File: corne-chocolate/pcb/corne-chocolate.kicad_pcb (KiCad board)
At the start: 2 copper layers, 116.2 x 91.4 mm, 82 parts, among them J1 MJ-4PP-9, J2 Conn_01x04, J3 Conn_01x03, P1 Conn_01x01, P2 Conn_01x01, SW10 SW_PUSH, SW11 SW_PUSH, SW12 SW_PUSH, SW14 SW_PUSH, SW15 SW_PUSH, SW16 SW_PUSH, SW17 SW_PUSH, SW18 SW_PUSH, SW19 SW_PUSH, SW2 SW_PUSH, SW20 SW_PUSH, SW21 SW_PUSH, SW3 SW_PUSH, SW4 SW_PUSH, SW5 SW_PUSH, SW6 SW_PUSH, SW8 SW_PUSH, SW9 SW_PUSH, U1 ProMicro

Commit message: finishes routing
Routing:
- added copper zone on B.Cu, net (none)
- removed copper zone on B.Cu, net Net-(D18-A)
- removed copper zone on B.Cu, net Net-(L12-DIN)
- removed copper zone on B.Cu, net Net-(L14-DOUT)

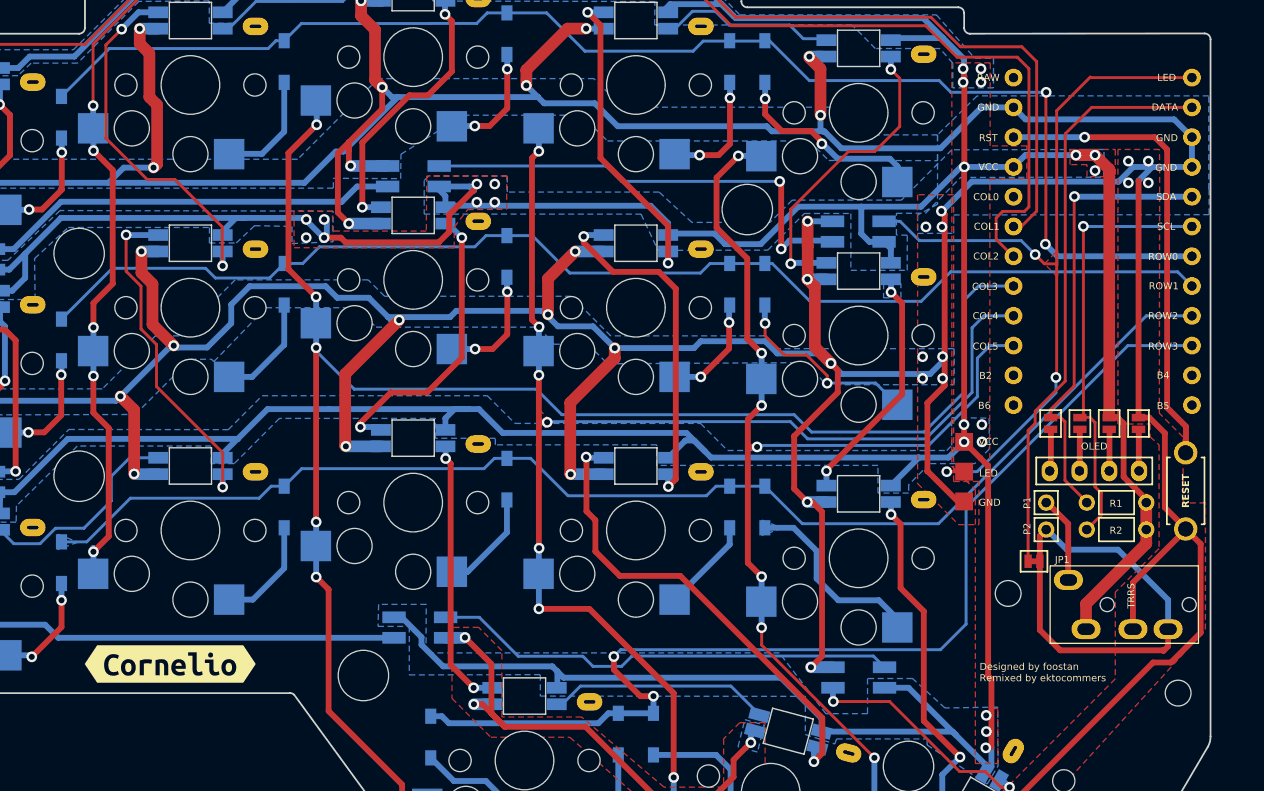
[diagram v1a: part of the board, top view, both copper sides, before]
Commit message: updates some footprints
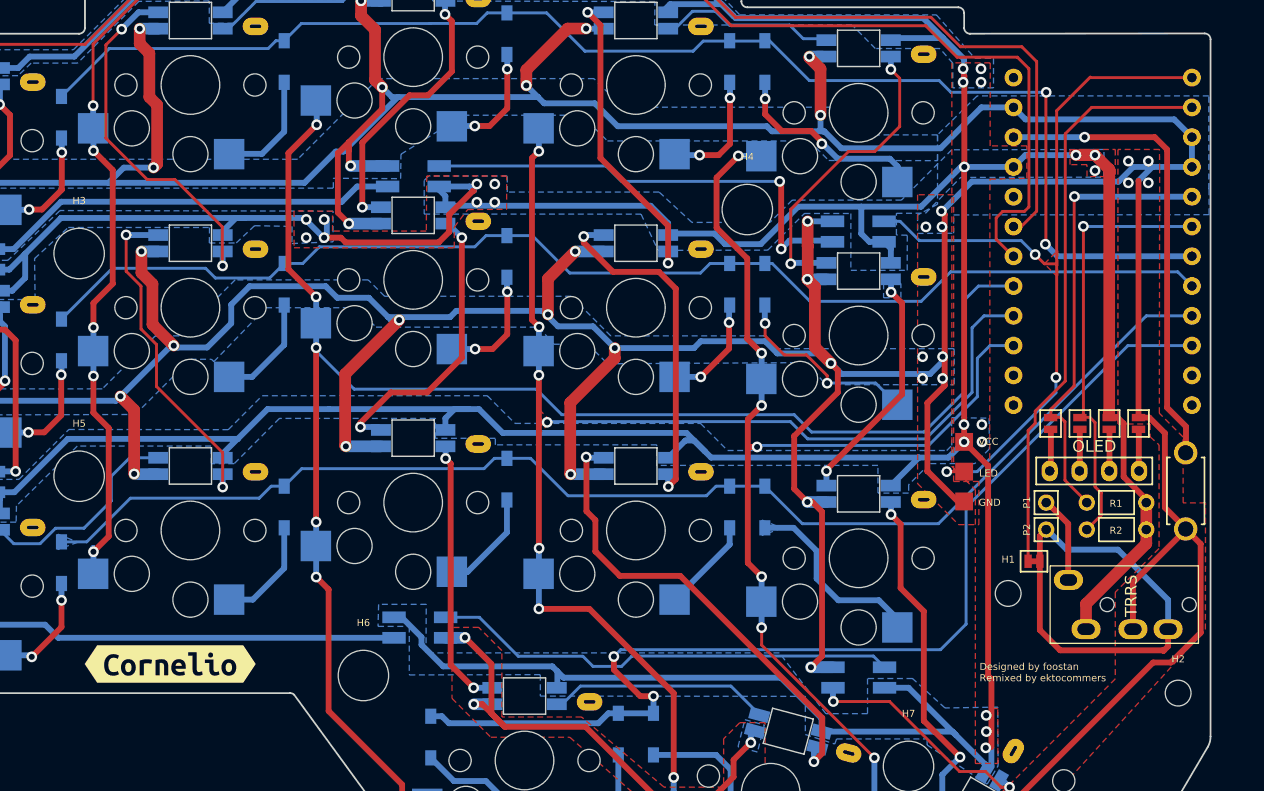
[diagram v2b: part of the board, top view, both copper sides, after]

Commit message: reannotates
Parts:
- removed J3: Conn_01x03, kbd:StripLED_1side
- removed JP1: Device:Jumper, kbd:Jumper
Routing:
- net LED: track 66.7 -> 39.2 mm, vias 3 -> 1
- net GND: track 639.5 -> 627.4 mm
- net data: track 88.0 -> 85.0 mm
- net row0: track 116.4 -> 116.9 mm
- net SCL: track 37.0 -> 36.5 mm
- removed copper zone on F.Cu, net LED
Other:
- board text removed: "GND"
- board text removed: "LED"
- board text removed: "VCC"

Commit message: starts component review
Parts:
- D10, D11, D12, D14, D15, D16, D17, D18, D19, D2, D20, D21, D3, D4, D5, D6, D8, D9: value D -> 1N4148W; footprint kbd:D3_SMD -> kbd:D_SOD-123
- moved D2 0.09 mm to (97.0, 75.2)

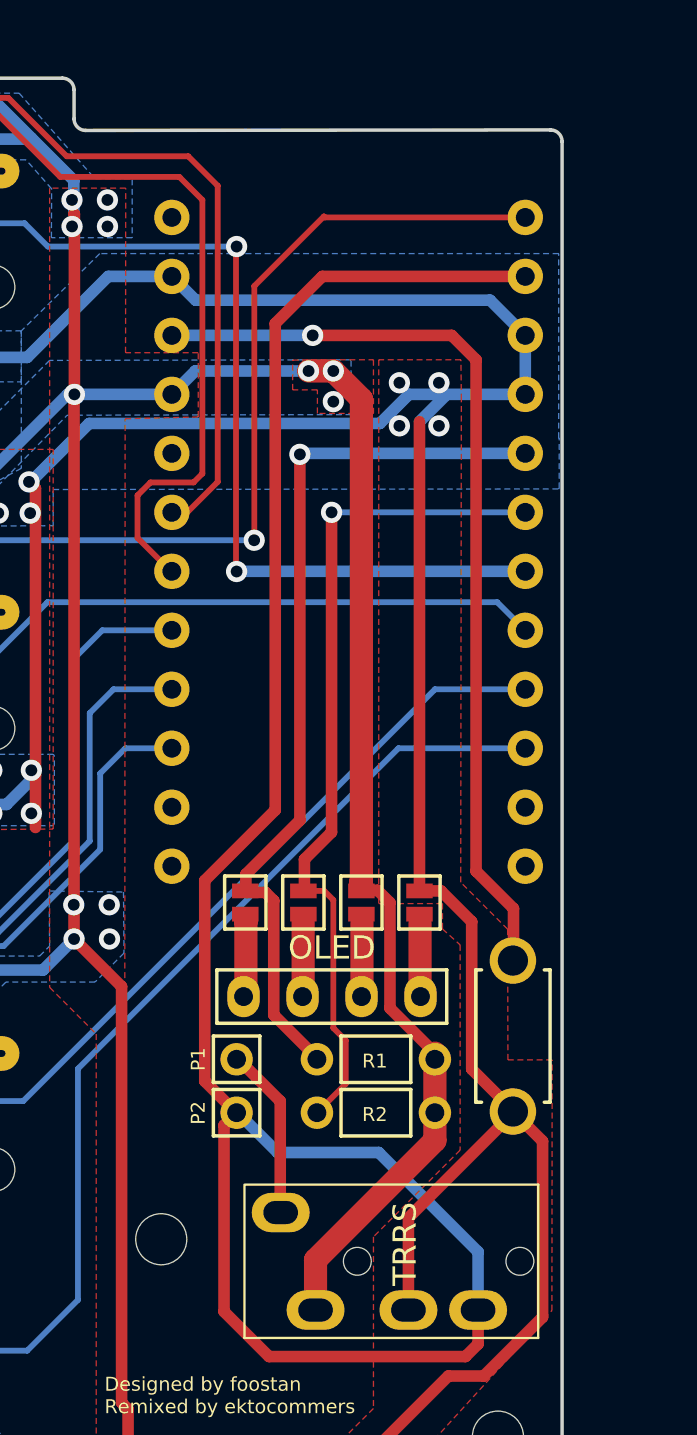
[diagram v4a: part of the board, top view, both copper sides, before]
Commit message: switch to nrf52840 micro. All items from amazon
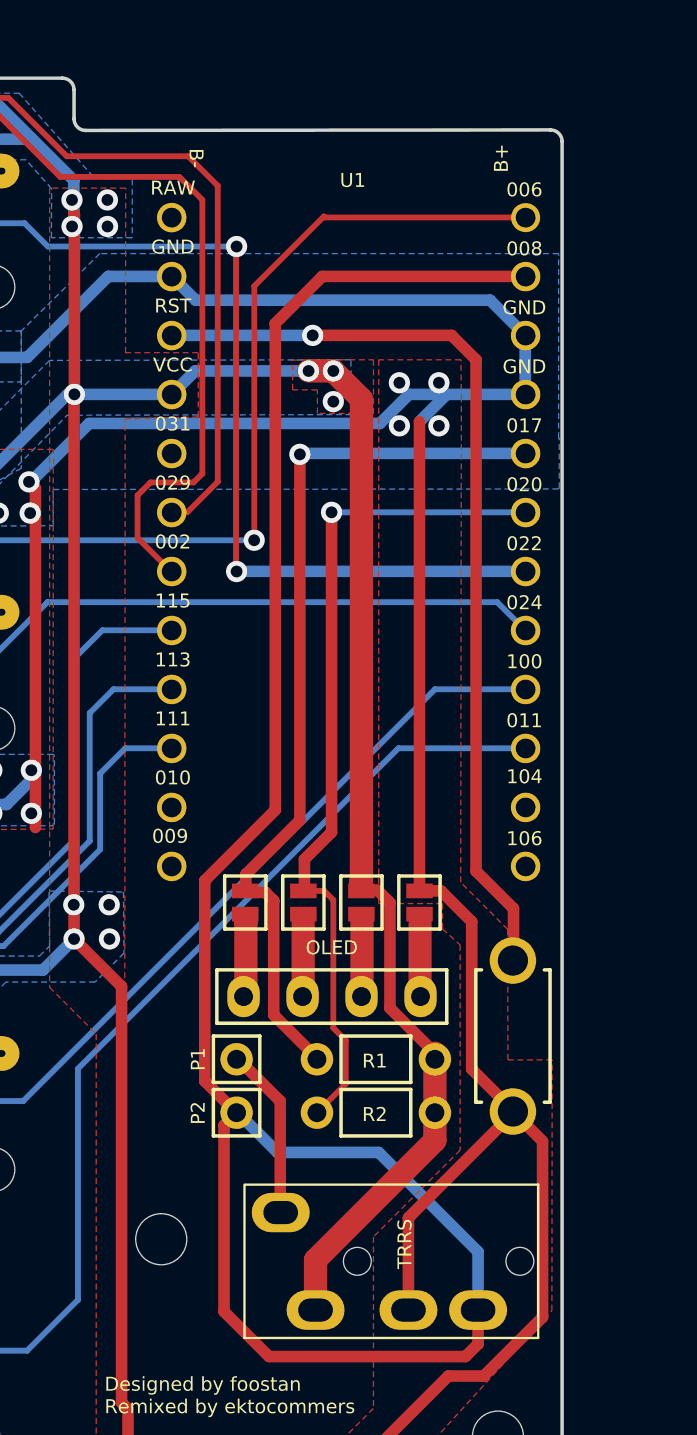
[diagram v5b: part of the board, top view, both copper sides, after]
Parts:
- U1: value ProMicro -> nrf52840; footprint kbd:ProMicro_v2_1side -> kbd:nrf52840
- moved U1 16.5 mm to (186.5, 102.7)

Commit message: adds right keyboard
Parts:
- added D13: 1N4148W, kbd:D_SOD-123, F.Cu at (247.7, 90.2)
- added D22: 1N4148W, kbd:D_SOD-123, F.Cu at (247.7, 109.2)
- added D23: 1N4148W, kbd:D_SOD-123, F.Cu at (228.7, 66.6)
- added D24: 1N4148W, kbd:D_SOD-123, F.Cu at (228.7, 85.5)
- added D25: 1N4148W, kbd:D_SOD-123, F.Cu at (228.7, 104.4)
- added D26: 1N4148W, kbd:D_SOD-123, F.Cu at (209.7, 64.2)
- added D27: 1N4148W, kbd:D_SOD-123, F.Cu at (209.7, 83.2)
- added D28: 1N4148W, kbd:D_SOD-123, F.Cu at (209.7, 102.0)
- added D29: 1N4148W, kbd:D_SOD-123, F.Cu at (216.2, 124.1)
- added D30: 1N4148W, kbd:D_SOD-123, F.Cu at (190.7, 66.5)
- added D31: 1N4148W, kbd:D_SOD-123, F.Cu at (190.7, 85.5)
- added D32: 1N4148W, kbd:D_SOD-123, F.Cu at (190.7, 104.5)
- added D33: 1N4148W, kbd:D_SOD-123, F.Cu at (200.2, 123.9)
- added D34: 1N4148W, kbd:D_SOD-123, F.Cu at (187.7, 66.4)
- added D35: 1N4148W, kbd:D_SOD-123, F.Cu at (187.7, 85.5)
- added D36: 1N4148W, kbd:D_SOD-123, F.Cu at (187.7, 104.4)
- added D37: 1N4148W, kbd:D_SOD-123, F.Cu at (197.2, 123.8)
- added D7: 1N4148W, kbd:D_SOD-123, F.Cu at (247.8, 71.3)
- added H10: MountingHole, MountingHole:MountingHole_2.2mm_M2_ISO14580, F.Cu at (152.5, 120.4)
- added H11: MountingHole, MountingHole:MountingHole_4.3mm_M4_ISO14580, F.Cu at (222.0, 118.9)
- added H12: MountingHole, MountingHole:MountingHole_2.2mm_M2_ISO14580, F.Cu at (167.0, 111.9)
- added H13: MountingHole, MountingHole:MountingHole_4.3mm_M4_ISO14580, F.Cu at (246.2, 101.9)
- added H14: MountingHole, MountingHole:MountingHole_4.3mm_M4_ISO14580, F.Cu at (246.2, 82.9)
- added H7, H8: MountingHole, MountingHole:MountingHole_4.3mm_M4_ISO14580, F.Cu at (175.5, 126.6)
- added H9: MountingHole, MountingHole:MountingHole_4.3mm_M4_ISO14580, F.Cu at (189.2, 79.1)
- added J3: MJ-4PP-9, kbd:MJ-4PP-9_1side, F.Cu at (150.0, 112.8)
- added J4: Conn_01x04, kbd:OLED_1side, F.Cu at (155.8, 101.4)
- added JP6: Device:Jumper_NO_Small, kbd:Jumper, F.Cu at (155.9, 97.4)
- added JP7: Device:Jumper_NO_Small, kbd:Jumper, F.Cu at (158.3, 97.4)
- added JP8: Device:Jumper_NO_Small, kbd:Jumper, F.Cu at (160.9, 97.4)
- added JP9: Device:Jumper_NO_Small, kbd:Jumper, F.Cu at (163.3, 97.4)
- added L10, L37: SK6812MINI, kbd:YS-SK6812MINI-E, F.Cu at (217.7, 79.6)
- added L13: SK6812MINI, kbd:YS-SK6812MINI-E, F.Cu at (255.7, 86.7)
- added L28: SK6812MINI, kbd:SK6812MINI_underglow_rev, F.Cu at (255.7, 83.4)
- added L29: SK6812MINI, kbd:SK6812MINI_underglow_rev, F.Cu at (255.7, 102.3)
- added L30: SK6812MINI, kbd:YS-SK6812MINI-E, F.Cu at (255.8, 105.8)
- added L31: SK6812MINI, kbd:YS-SK6812MINI-E, F.Cu at (236.7, 62.9)
- added L32: SK6812MINI, kbd:YS-SK6812MINI-E, F.Cu at (236.7, 82.0)
- added L33: SK6812MINI, kbd:YS-SK6812MINI-E, F.Cu at (236.8, 101.0)
- added L34: SK6812MINI, kbd:SK6812MINI_underglow_rev, F.Cu at (217.7, 76.3)
- added L35: SK6812MINI, kbd:SK6812MINI_underglow_rev, F.Cu at (217.2, 114.8)
- added L36: SK6812MINI, kbd:YS-SK6812MINI-E, F.Cu at (217.8, 60.6)
- added L38: SK6812MINI, kbd:YS-SK6812MINI-E, F.Cu at (217.8, 98.6)
- added L39: SK6812MINI, kbd:YS-SK6812MINI-E, F.Cu at (208.3, 120.6)
- added L4: SK6812MINI, kbd:YS-SK6812MINI-E, F.Cu at (217.7, 60.6)
- added L40: SK6812MINI, kbd:YS-SK6812MINI-E, F.Cu at (198.7, 62.9)
- added L41: SK6812MINI, kbd:YS-SK6812MINI-E, F.Cu at (198.8, 82.0)
- added L42: SK6812MINI, kbd:YS-SK6812MINI-E, F.Cu at (198.7, 100.9)
- added L43: SK6812MINI, kbd:YS-SK6812MINI-E, F.Cu at (185.7, 123.6)
- added L44: SK6812MINI, kbd:SK6812MINI_underglow_rev, F.Cu at (179.8, 81.0)
- added L45: SK6812MINI, kbd:SK6812MINI_underglow_rev, F.Cu at (179.7, 119.0)
- added L46: SK6812MINI, kbd:YS-SK6812MINI-E, F.Cu at (179.7, 65.4)
- added L47: SK6812MINI, kbd:YS-SK6812MINI-E, F.Cu at (179.7, 84.4)
- added L48: SK6812MINI, kbd:YS-SK6812MINI-E, F.Cu at (179.7, 103.4)
- added L49: SK6812MINI, kbd:YS-SK6812MINI-E, F.Cu at (169.7, 129.9)
- added L5: SK6812MINI, kbd:YS-SK6812MINI-E, F.Cu at (198.7, 63.0)
- added L7: SK6812MINI, kbd:YS-SK6812MINI-E, F.Cu at (255.7, 67.7)
- added P3: Conn_01x01, kbd:1pin_conn, F.Cu at (163.7, 104.1)
- added P4: Conn_01x01, kbd:1pin_conn, F.Cu at (163.7, 106.4)
- added R3: R, kbd:R, F.Cu at (157.7, 104.1)
- added R4: R, kbd:R, F.Cu at (157.7, 106.4)
- added RSW2: SW_PUSH, kbd:ResetSW_1side, F.Cu at (151.8, 103.1)
- added SW13: SW_PUSH, kbd:ChocV1_V2_Hotswap, F.Cu at (255.7, 92.2)
- added SW22: SW_PUSH, kbd:ChocV1_V2_Hotswap, F.Cu at (255.7, 111.2)
- added SW23: SW_PUSH, kbd:ChocV1_V2_Hotswap, F.Cu at (236.7, 68.5)
- added SW24: SW_PUSH, kbd:ChocV1_V2_Hotswap, F.Cu at (236.7, 87.5)
- added SW25: SW_PUSH, kbd:ChocV1_V2_Hotswap, F.Cu at (236.7, 106.5)
- added SW26: SW_PUSH, kbd:ChocV1_V2_Hotswap, F.Cu at (217.7, 66.1)
- added SW27: SW_PUSH, kbd:ChocV1_V2_Hotswap, F.Cu at (217.7, 85.1)
- added SW28: SW_PUSH, kbd:ChocV1_V2_Hotswap, F.Cu at (217.7, 104.1)
- added SW29: SW_PUSH, kbd:ChocV1_V2_Hotswap, F.Cu at (208.2, 126.1)
- added SW30: SW_PUSH, kbd:ChocV1_V2_Hotswap, F.Cu at (198.7, 68.5)
- added SW31: SW_PUSH, kbd:ChocV1_V2_Hotswap, F.Cu at (198.7, 87.5)
- added SW32: SW_PUSH, kbd:ChocV1_V2_Hotswap, F.Cu at (198.7, 106.5)
- added SW33: SW_PUSH, kbd:ChocV1_V2_Hotswap, F.Cu at (187.2, 128.9)
- added SW34: SW_PUSH, kbd:ChocV1_V2_Hotswap, F.Cu at (179.7, 70.9)
- added SW35: SW_PUSH, kbd:ChocV1_V2_Hotswap, F.Cu at (179.7, 89.9)
- added SW36: SW_PUSH, kbd:ChocV1_V2_Hotswap, F.Cu at (179.7, 108.9)
- added SW37: SW_PUSH, kbd:ChocV1_V2_Hotswap_1.5u, F.Cu at (165.0, 132.6)
- added SW7: SW_PUSH, kbd:ChocV1_V2_Hotswap, F.Cu at (255.7, 73.2)
- added U2: ProMicro, kbd:ProMicro_v2_1side, F.Cu at (158.9, 82.3)
- added kibuzzard-65BBD98A: G***, kibuzzard-65BBD98A, F.Cu at (238.5, 117.9)
- U1: value nrf52840 -> ProMicro; footprint kbd:nrf52840 -> kbd:ProMicro_v2_1side
- moved U1 54.1 mm to (136.4, 82.3)
- moved kibuzzard-65BBD98A 49.5 mm to (56.9, 117.9)
- moved D10 49.5 mm to (85.6, 83.1)
- moved D11 49.5 mm to (104.6, 85.5)
- moved D12 49.5 mm to (107.6, 85.5)
- moved D14 49.5 mm to (47.6, 109.2)
- moved D15 49.5 mm to (66.6, 104.5)
- moved D16 49.5 mm to (85.6, 102.1)
- moved D17 49.5 mm to (104.6, 104.5)
- moved D18 49.5 mm to (107.6, 104.5)
- moved D19 49.5 mm to (79.1, 124.1)
- moved D2 49.5 mm to (47.6, 71.3)
- moved D20 49.5 mm to (95.1, 123.9)
- moved D21 49.5 mm to (98.1, 123.9)
- moved D3 49.5 mm to (66.6, 66.5)
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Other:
- board size 116.2 x 91.4 mm -> 236.4 x 91.4 mm
- board text added: "#61127AFF"
- board text added: "0"
- board text added: "0 mm"
- board text added: "0.02"
- board text added: "0.0254 mm"
- board text added: "0.03556 mm"
- board text added: "0.1524 mm / 0.1524 mm"
- board text added: "0.2540 mm"
- board text added: "1"
- board text added: "1.524 mm"
- board text added: "1.6459 mm"
- board text added: "2"
- board text added: "236.3514 mm x 91.3949 mm"
- board text added: "3.3"
- board text added: "4.5"
- board text added: "B.Cu"
- board text added: "B.Mask"
- board text added: "B.Paste"
- board text added: "B.Silkscreen"
- board text added: "BOARD CHARACTERISTICS"
- board text added: "Board Thickness:"
- board text added: "Board overall dimensions:"
- board text added: "Bottom Silk Screen"
- board text added: "Bottom Solder Mask"
- board text added: "Bottom Solder Paste"
- board text added: "Castellated pads:"
- board text added: "Color"
- board text added: "Copper Finish:"
- board text added: "Copper Layer Count:"
- board text added: "Dielectric"
- board text added: "ENIG"
- board text added: "Edge card connectors:"
- board text added: "Epsilon R"
- board text added: "F.Cu"
- board text added: "F.Mask"
- board text added: "F.Paste"
- board text added: "F.Silkscreen"
- board text added: "FR4"
- board text added: "FR4 natural"
- board text added: "Impedance Control:"
- board text added: "Layer Name"
- board text added: "Loss Tangent"
- board text added: "Material"
- board text added: "Min hole diameter:"
- board text added: "Min track/spacing:"
- board text added: "No"
- board text added: "Not specified"
- board text added: "Plated Board Edge:"
- board text added: "Thickness (mm)"
- board text added: "Top Silk Screen"
- board text added: "Top Solder Mask"
- board text added: "Top Solder Paste"
- board text added: "Type"
- board text added: "White"
- board text added: "copper"
- board text added: "core"

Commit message: adds right board. stars routing
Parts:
- removed the H7 at (175.5, 126.6)
- removed the L10 at (217.7, 79.6)
- removed the L4 at (217.7, 60.6)
- removed the L5 at (198.7, 63.0)
- moved J4 7.59 mm to (163.4, 101.4), turned to 180 degrees
- turned L13 to 180 degrees
- turned L28 to 180 degrees
- turned L33 to 180 degrees
- turned L34 to 180 degrees
- turned L36 to 180 degrees
- turned L37 to 180 degrees
- turned L43 to -150 degrees
- turned L44 to 180 degrees
- turned L46 to 180 degrees
- turned L49 to 125 degrees
- turned SW33 to 15 degrees
- turned SW37 to -60 degrees
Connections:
- D10 pad 1: row1 -> Lrow1
- D11 pad 1: row1 -> Lrow1
- D12 pad 1: row1 -> Lrow1
- D13 pad 1: row1 -> Rrow1
- D14 pad 1: row2 -> Lrow2
- D15 pad 1: row2 -> Lrow2
- D16 pad 1: row2 -> Lrow2
- D17 pad 1: row2 -> Lrow2
- D18 pad 1: row2 -> Lrow2
- D19 pad 1: row3 -> Lrow3
- D2 pad 1: row0 -> Lrow0
- D20 pad 1: row3 -> Lrow3
- D21 pad 1: row3 -> Lrow3
- D22 pad 1: row2 -> Rrow2
- D23 pad 1: row0 -> Rrow0
- D24 pad 1: row1 -> Rrow1
- D25 pad 1: row2 -> Rrow2
- D26 pad 1: row0 -> Rrow0
- D27 pad 1: row1 -> Rrow1
- D28 pad 1: row2 -> Rrow2
- D29 pad 1: row3 -> Rrow3
- D3 pad 1: row0 -> Lrow0
- D30 pad 1: row0 -> Rrow0
- D31 pad 1: row1 -> Rrow1
- D32 pad 1: row2 -> Rrow2
- D33 pad 1: row3 -> Rrow3
- D34 pad 1: row0 -> Rrow0
- D35 pad 1: row1 -> Rrow1
- D36 pad 1: row2 -> Rrow2
- D37 pad 1: row3 -> Rrow3
- D4 pad 1: row0 -> Lrow0
- D5 pad 1: row0 -> Lrow0
- D6 pad 1: row0 -> Lrow0
- D7 pad 1: row0 -> Rrow0
- D8 pad 1: row1 -> Lrow1
- D9 pad 1: row1 -> Lrow1
- J1 pad B: data -> Ldata
- J1 pad C: GND -> LGND
- J1 pad D: VCC -> LVCC
- J3 pad B: data -> Rdata
- J3 pad C: GND -> RGND
- J3 pad D: VCC -> RVCC
- JP2 pad 2: GND -> LGND
- JP3 pad 1: VCC -> LVCC
- JP4 pad 1: SCL -> LSCL
- JP5 pad 1: SDA -> LSDA
- JP6 pad 2: GND -> RGND
- JP7 pad 1: VCC -> RVCC
- JP8 pad 1: SCL -> RSCL
- JP9 pad 1: SDA -> RSDA
- L10 pad 2: GND -> LGND
- L10 pad 4: VCC -> LVCC
- L11 pad 2: GND -> LGND
- L11 pad 4: VCC -> LVCC
- L12 pad 2: GND -> LGND
- L12 pad 4: VCC -> LVCC
- L13 pad 2: GND -> RGND
- L13 pad 4: VCC -> RVCC
- L14 pad 2: GND -> LGND
- L14 pad 4: VCC -> LVCC
- L15 pad 2: GND -> LGND
- L15 pad 4: VCC -> LVCC
- L16 pad 2: GND -> LGND
- L16 pad 4: VCC -> LVCC
- L17 pad 2: GND -> LGND
- L17 pad 4: VCC -> LVCC
- L18 pad 2: GND -> LGND
- L18 pad 4: VCC -> LVCC
- L19 pad 2: GND -> LGND
- L19 pad 4: VCC -> LVCC
- L2 pad 2: GND -> LGND
- L2 pad 4: VCC -> LVCC
- L20 pad 2: GND -> LGND
- L20 pad 4: VCC -> LVCC
- L21 pad 2: GND -> LGND
- L21 pad 4: VCC -> LVCC
- L22 pad 2: GND -> LGND
- L22 pad 4: VCC -> LVCC
- L23 pad 2: GND -> LGND
- L23 pad 4: VCC -> LVCC
- L24 pad 2: GND -> LGND
- L24 pad 3: LED -> LLED
- L24 pad 4: VCC -> LVCC
- L25 pad 2: GND -> LGND
- L25 pad 4: VCC -> LVCC
- L26 pad 2: GND -> LGND
- L26 pad 4: VCC -> LVCC
- L27 pad 2: GND -> LGND
- L27 pad 4: VCC -> LVCC
- L28 pad 2: GND -> RGND
- L28 pad 4: VCC -> RVCC
- L29 pad 2: GND -> RGND
- L29 pad 4: VCC -> RVCC
- L3 pad 2: GND -> LGND
- L3 pad 4: VCC -> LVCC
- L30 pad 2: GND -> RGND
- L30 pad 4: VCC -> RVCC
- L31 pad 2: GND -> RGND
- L31 pad 4: VCC -> RVCC
- L32 pad 2: GND -> RGND
- L32 pad 4: VCC -> RVCC
- L33 pad 2: GND -> RGND
- L33 pad 4: VCC -> RVCC
- L34 pad 2: GND -> RGND
- L34 pad 4: VCC -> RVCC
- L35 pad 2: GND -> RGND
- L35 pad 4: VCC -> RVCC
- L36 pad 2: GND -> RGND
- L36 pad 4: VCC -> RVCC
- L37 pad 2: GND -> RGND
- L37 pad 4: VCC -> RVCC
- L38 pad 2: GND -> RGND
- L38 pad 4: VCC -> RVCC
- L39 pad 2: GND -> RGND
- L39 pad 4: VCC -> RVCC
- L4 pad 2: GND -> LGND
- L4 pad 4: VCC -> LVCC
- L40 pad 2: GND -> RGND
- L40 pad 4: VCC -> RVCC
- L41 pad 2: GND -> RGND
- L41 pad 4: VCC -> RVCC
- L42 pad 2: GND -> RGND
- L42 pad 4: VCC -> RVCC
- L43 pad 2: GND -> RGND
- L43 pad 4: VCC -> RVCC
- L44 pad 2: GND -> RGND
- L44 pad 3: LED -> RLED
- L44 pad 4: VCC -> RVCC
- L45 pad 2: GND -> RGND
- L45 pad 4: VCC -> RVCC
- L46 pad 2: GND -> RGND
- L46 pad 4: VCC -> RVCC
- L47 pad 2: GND -> RGND
- L47 pad 4: VCC -> RVCC
- L48 pad 2: GND -> RGND
- L48 pad 4: VCC -> RVCC
- L49 pad 2: GND -> RGND
- L49 pad 4: VCC -> RVCC
- L5 pad 2: GND -> LGND
- L5 pad 4: VCC -> LVCC
- L6 pad 2: GND -> LGND
- L6 pad 4: VCC -> LVCC
- L7 pad 2: GND -> RGND
- L7 pad 4: VCC -> RVCC
- L8 pad 2: GND -> LGND
- L8 pad 4: VCC -> LVCC
- L9 pad 2: GND -> LGND
- L9 pad 4: VCC -> LVCC
- P2 pad 1: data -> Ldata
- P4 pad 1: data -> Rdata
- R1 pad 1: VCC -> LVCC
- R1 pad 2: SDA -> LSDA
- R2 pad 1: VCC -> LVCC
- R2 pad 2: SCL -> LSCL
- R3 pad 1: VCC -> RVCC
- R3 pad 2: SDA -> RSDA
- R4 pad 1: VCC -> RVCC
- R4 pad 2: SCL -> RSCL
- RSW1 pad 1: reset -> Lreset
- RSW1 pad 2: GND -> LGND
- RSW2 pad 1: reset -> Rreset
- RSW2 pad 2: GND -> RGND
- SW10 pad 1: col3 -> Lcol3
- SW11 pad 1: col4 -> Lcol4
- SW12 pad 1: col5 -> Lcol5
- SW13 pad 1: col1 -> Rcol1
- SW14 pad 1: col1 -> Lcol1
- SW15 pad 1: col2 -> Lcol2
- SW16 pad 1: col3 -> Lcol3
- SW17 pad 1: col4 -> Lcol4
- SW18 pad 1: col5 -> Lcol5
- SW19 pad 1: col3 -> Lcol3
- SW2 pad 1: col1 -> Lcol1
- SW20 pad 1: col4 -> Lcol4
- SW21 pad 1: col5 -> Lcol5
- SW22 pad 1: col1 -> Rcol1
- SW23 pad 1: col2 -> Rcol2
- SW24 pad 1: col2 -> Rcol2
- SW25 pad 1: col2 -> Rcol2
- SW26 pad 1: col3 -> Rcol3
- SW27 pad 1: col3 -> Rcol3
- SW28 pad 1: col3 -> Rcol3
- SW29 pad 1: col3 -> Rcol3
- SW3 pad 1: col2 -> Lcol2
- SW30 pad 1: col4 -> Rcol4
- SW31 pad 1: col4 -> Rcol4
- SW32 pad 1: col4 -> Rcol4
- SW33 pad 1: col4 -> Rcol4
- SW34 pad 1: col5 -> Rcol5
- SW35 pad 1: col5 -> Rcol5
- SW36 pad 1: col5 -> Rcol5
- SW37 pad 1: col5 -> Rcol5
- SW4 pad 1: col3 -> Lcol3
- SW5 pad 1: col4 -> Lcol4
- SW6 pad 1: col5 -> Lcol5
- SW7 pad 1: col1 -> Rcol1
- SW8 pad 1: col1 -> Lcol1
- SW9 pad 1: col2 -> Lcol2
- U1 pad 1: LED -> LLED
- U1 pad 10: row3 -> Lrow3
- U1 pad 15: col5 -> Lcol5
- U1 pad 16: col4 -> Lcol4
- U1 pad 17: col3 -> Lcol3
- U1 pad 18: col2 -> Lcol2
- U1 pad 19: col1 -> Lcol1
- U1 pad 2: data -> Ldata
- U1 pad 21: VCC -> LVCC
- U1 pad 22: reset -> Lreset
- U1 pad 23: GND -> LGND
- U1 pad 3: GND -> LGND
- U1 pad 4: GND -> LGND
- U1 pad 5: SDA -> LSDA
- U1 pad 6: SCL -> LSCL
- U1 pad 7: row0 -> Lrow0
- U1 pad 8: row1 -> Lrow1
- U1 pad 9: row2 -> Lrow2
- U2 pad 1: LED -> RLED
- U2 pad 10: row3 -> Rrow3
- U2 pad 15: col5 -> Rcol5
- U2 pad 16: col4 -> Rcol4
- U2 pad 17: col3 -> Rcol3
- U2 pad 18: col2 -> Rcol2
- U2 pad 19: col1 -> Rcol1
- U2 pad 2: data -> Rdata
- U2 pad 21: VCC -> RVCC
- U2 pad 22: reset -> Rreset
- U2 pad 23: GND -> RGND
- U2 pad 3: GND -> RGND
- U2 pad 4: GND -> RGND
- U2 pad 5: SDA -> RSDA
- U2 pad 6: SCL -> RSCL
- U2 pad 7: row0 -> Rrow0
- U2 pad 8: row1 -> Rrow1
- U2 pad 9: row2 -> Rrow2
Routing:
- net LGND: track 0.00 -> 627.4 mm, vias 0 -> 42
- net GND: track 627.4 -> 0.00 mm, vias 42 -> 0
- net RVCC: track 0.00 -> 540.7 mm, vias 0 -> 9
- net VCC: track 511.7 -> 0.00 mm, vias 23 -> 0
- net LVCC: track 0.00 -> 511.7 mm, vias 0 -> 23
- net RGND: track 0.00 -> 497.3 mm, vias 0 -> 30
- net Rcol1: track 0.00 -> 175.0 mm, vias 0 -> 3
- net col1: track 169.4 -> 0.00 mm, vias 1 -> 0
- net Lcol1: track 0.00 -> 169.4 mm, vias 0 -> 1
- net col2: track 153.0 -> 0.00 mm, vias 5 -> 0
- net Lcol2: track 0.00 -> 153.0 mm, vias 0 -> 5
- net Rcol2: track 0.00 -> 148.4 mm, vias 0 -> 3
- net col3: track 140.2 -> 0.00 mm, vias 6 -> 0
- net Lcol3: track 0.00 -> 140.2 mm, vias 0 -> 6
- net Rcol3: track 0.00 -> 134.7 mm, vias 0 -> 4
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- added copper zone on B.Cu, net LGND
- added copper zone on F.Cu, net LGND
- added copper zone on B.Cu, net LVCC
- added copper zone on F.Cu, net LVCC
- added copper zone on F.Cu, net Lcol4
- added copper zone on B.Cu, net Lrow2
- removed copper zone on B.Cu, net GND
- removed copper zone on F.Cu, net GND
- removed copper zone on B.Cu, net VCC
- removed copper zone on F.Cu, net VCC
- removed copper zone on F.Cu, net col4
- removed copper zone on B.Cu, net row2
